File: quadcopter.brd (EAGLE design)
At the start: 130.1 x 130.1 mm, 75 parts, among them J1 AVR_SPI_PRG_6NS, J3 HEADER-0.1IN-2POS-FEMALE, J4 HEADER-0.1IN-2POS-FEMALE, J5 HEADER-0.1IN-2POS-FEMALE, J6 HEADER-0.1IN-2POS-FEMALE, SW1 PUSHBUTTON_SMD-VERTICAL, SW2 PUSHBUTTON_SMD-VERTICAL, U1 ATMEGA128RFA1

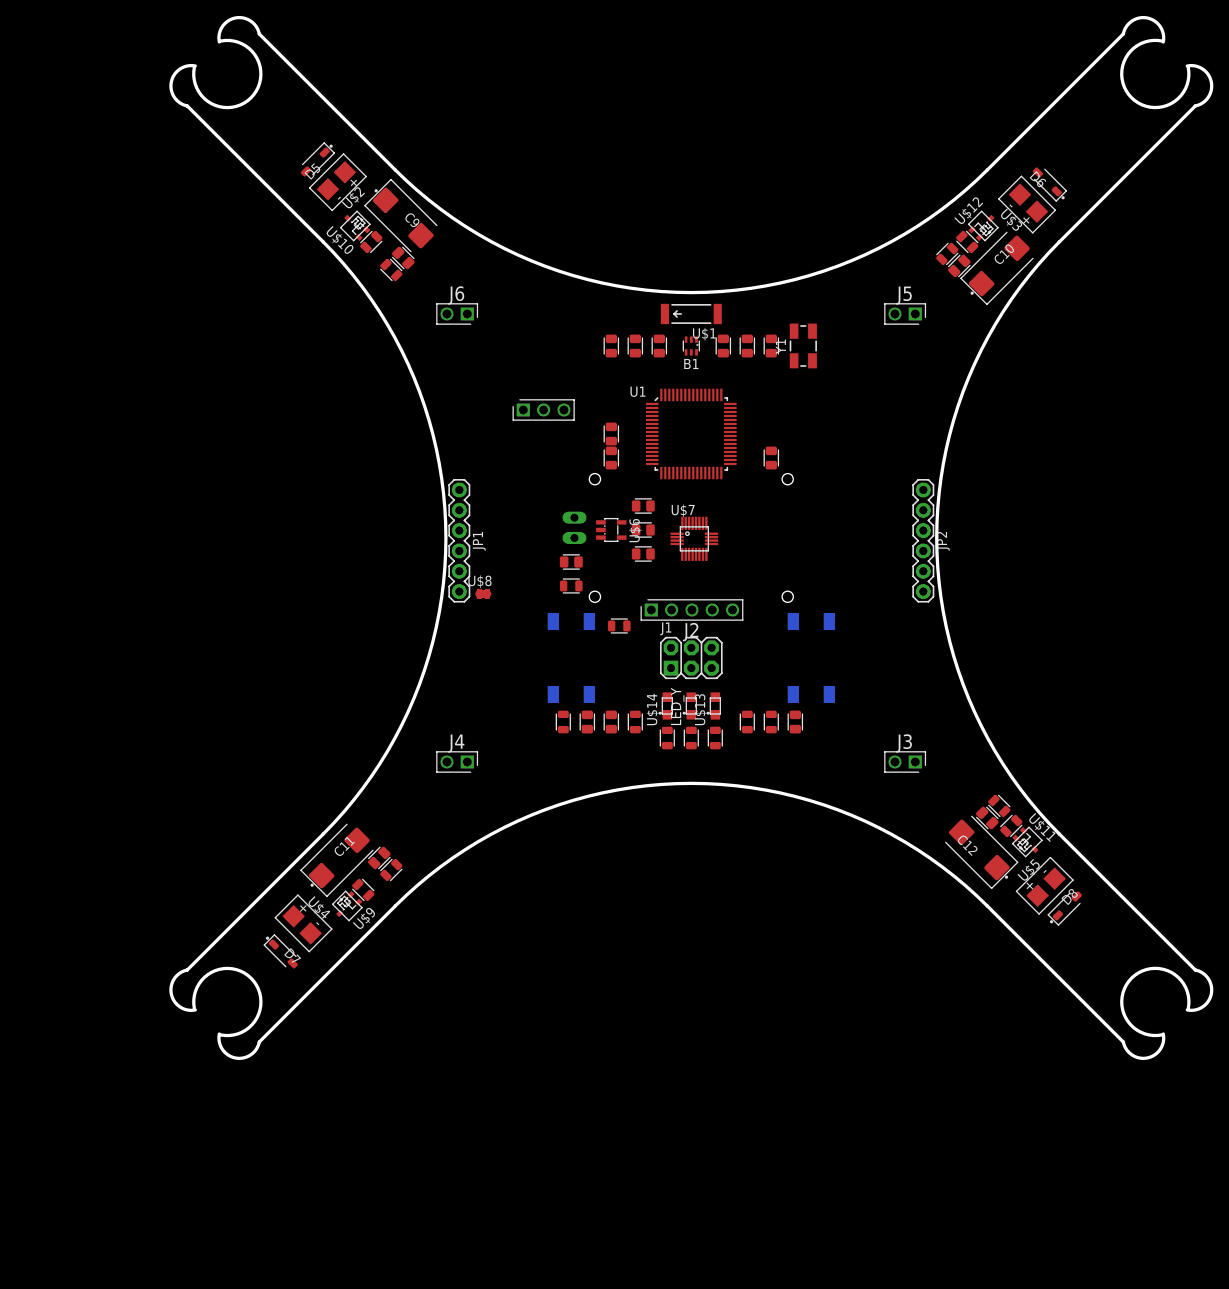
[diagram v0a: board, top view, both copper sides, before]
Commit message: Fixed n-fet and imu packages
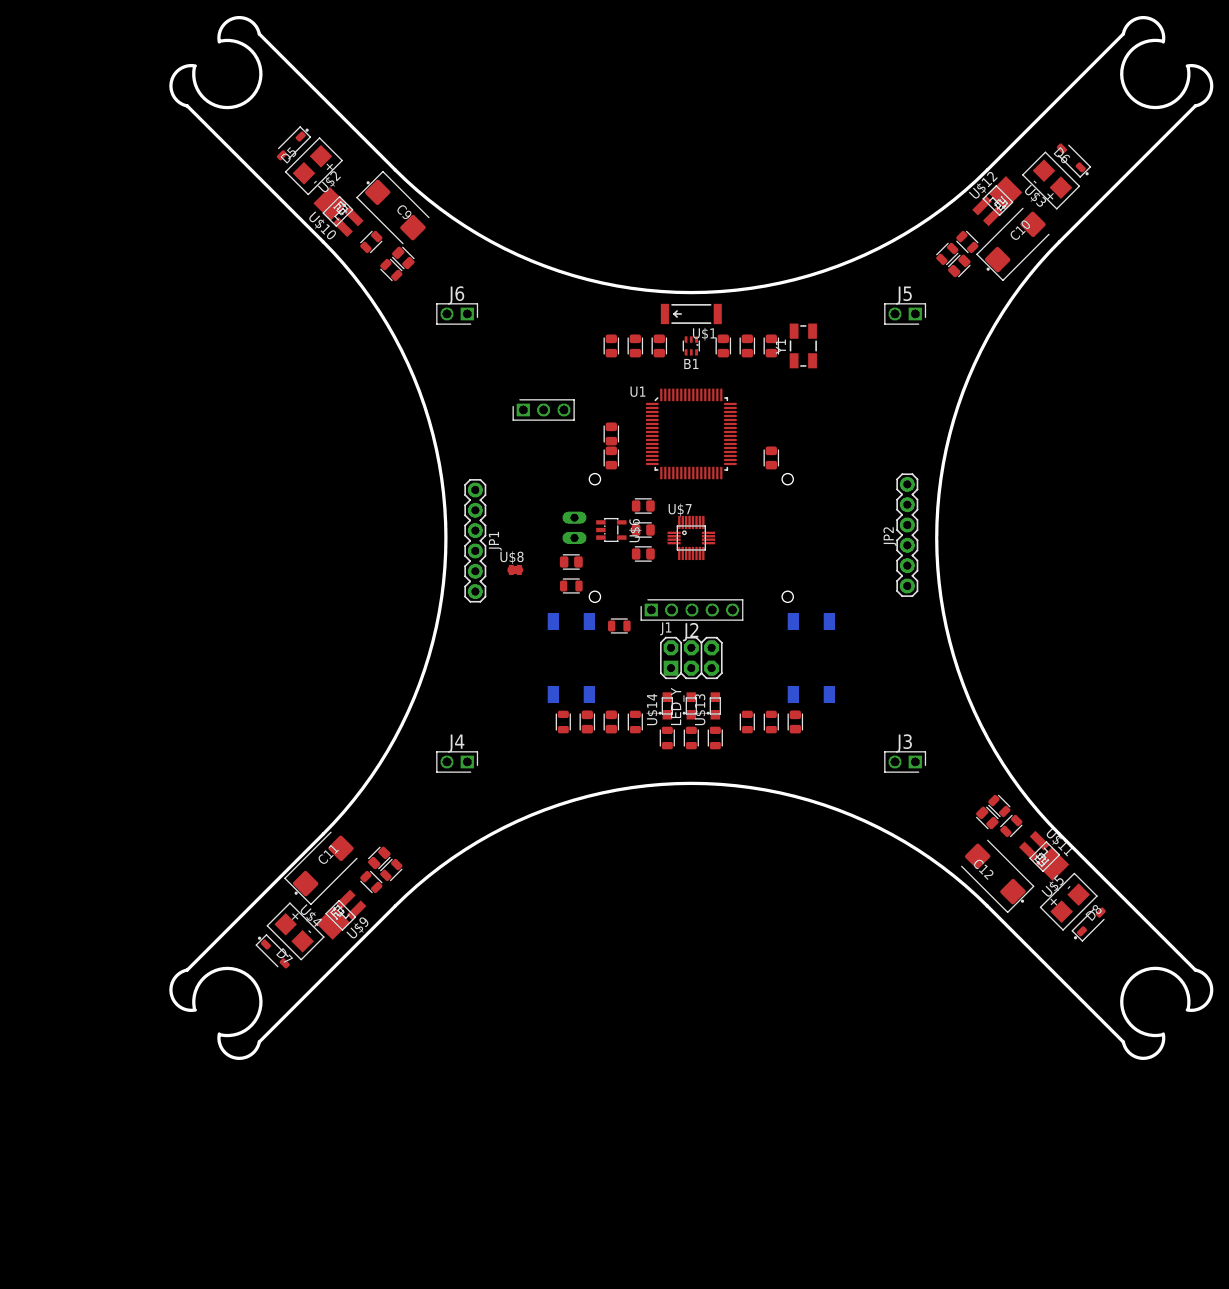
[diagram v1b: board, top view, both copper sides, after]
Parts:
- moved JP2 12.2 mm to (27.0, -6.00), turned to 90 degrees
- moved U$8 5.00 mm to (-22.0, -4.00)
- moved D6 4.24 mm to (47.5, 47.5)
- moved U$3 4.24 mm to (45.5, 44.5)
- moved C10 3.61 mm to (40.5, 37.0)
- moved C12 3.61 mm to (38.0, -42.0)
- moved D5 3.61 mm to (-50.0, 49.0)
- moved D8 3.61 mm to (50.0, -48.0)
- moved U$12 3.61 mm to (38.5, 42.0)
- moved U$2 3.61 mm to (-47.0, 47.0)
- moved U$5 3.61 mm to (47.0, -46.0)
- moved U$10 2.83 mm to (-44.0, 41.0)
- moved U$11 2.83 mm to (44.0, -40.0)
- moved C11 2.24 mm to (-46.0, -41.0)
- moved JP1 2.00 mm to (-27.0, 6.00)
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
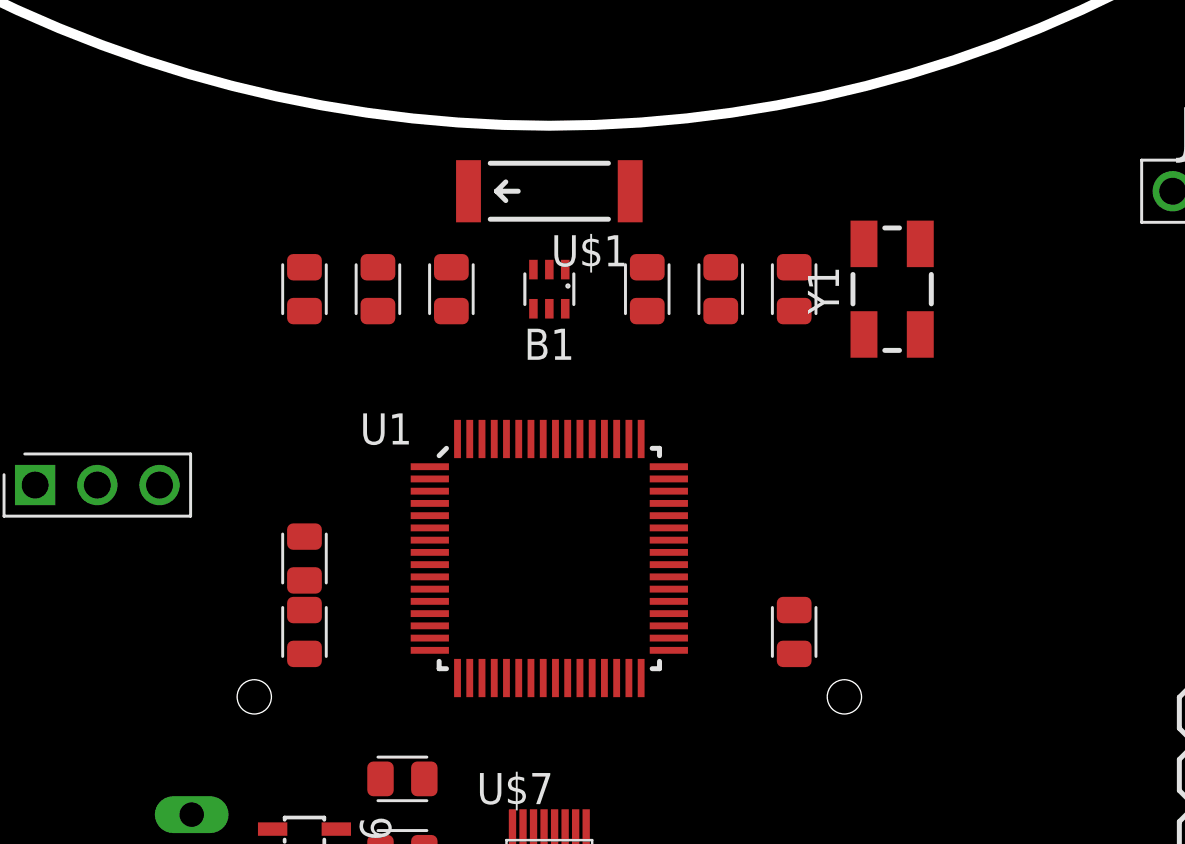
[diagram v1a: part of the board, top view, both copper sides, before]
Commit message: routed radio
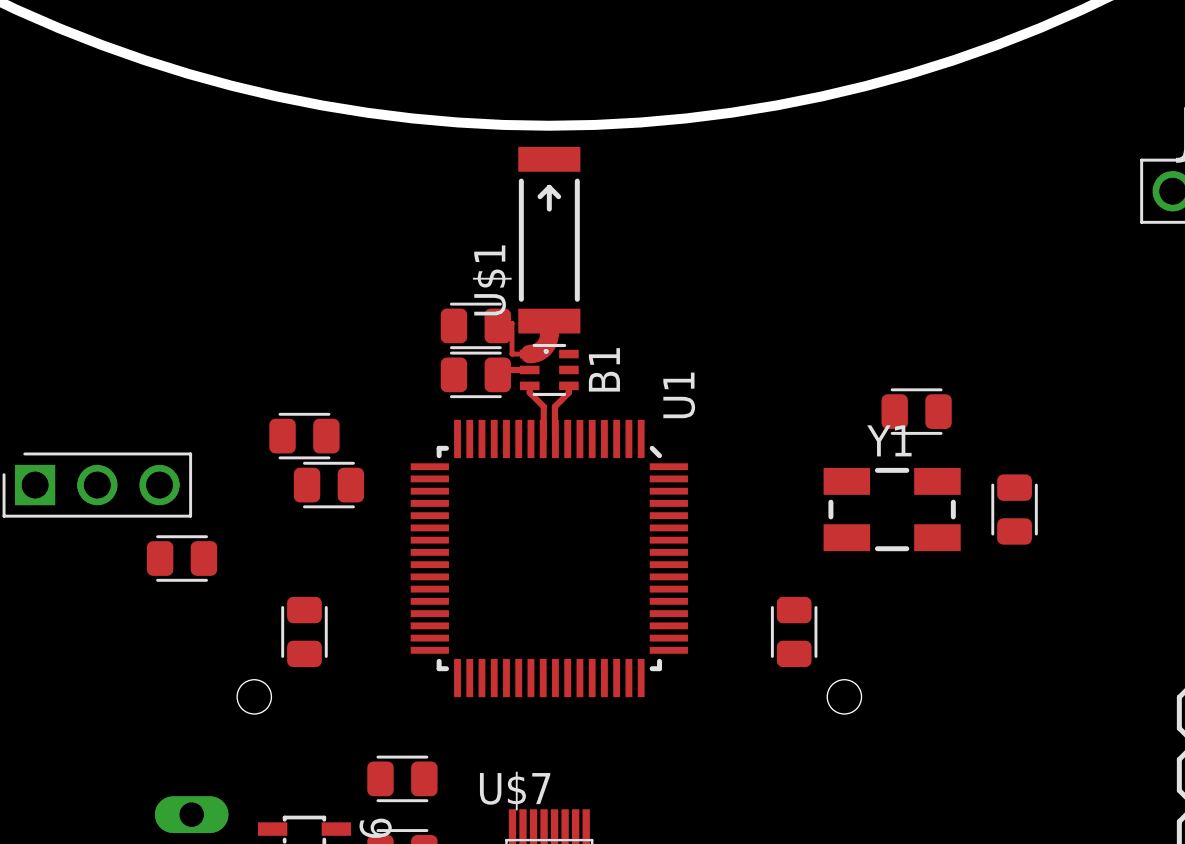
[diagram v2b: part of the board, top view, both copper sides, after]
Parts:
- moved C23 27.5 mm to (19.0, 15.0)
- moved C24 17.9 mm to (-9.00, 16.0), turned to 180 degrees
- moved Y1 9.00 mm to (14.0, 15.0), turned to 0 degrees
- moved C2 7.16 mm to (-3.00, 22.5), turned to 180 degrees
- moved C22 7.07 mm to (15.0, 19.0), turned to 180 degrees
- moved C25 6.00 mm to (-10.0, 18.0), turned to 0 degrees
- moved C4 5.00 mm to (-15.0, 13.0), turned to 0 degrees
- moved C1 3.64 mm to (-3.00, 20.5), turned to 0 degrees
- moved B1 3.30 mm to (0.00, 20.7), turned to 270 degrees
- moved U$1 2.00 mm to (0.00, 26.0), turned to 90 degrees
- turned U1 to 270 degrees
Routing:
- net ATTENNA: track 0.00 -> 4.35 mm
- net RFP: track 0.00 -> 2.41 mm
- net RFN: track 0.00 -> 2.41 mm
- net N$3: track 0.00 -> 1.50 mm

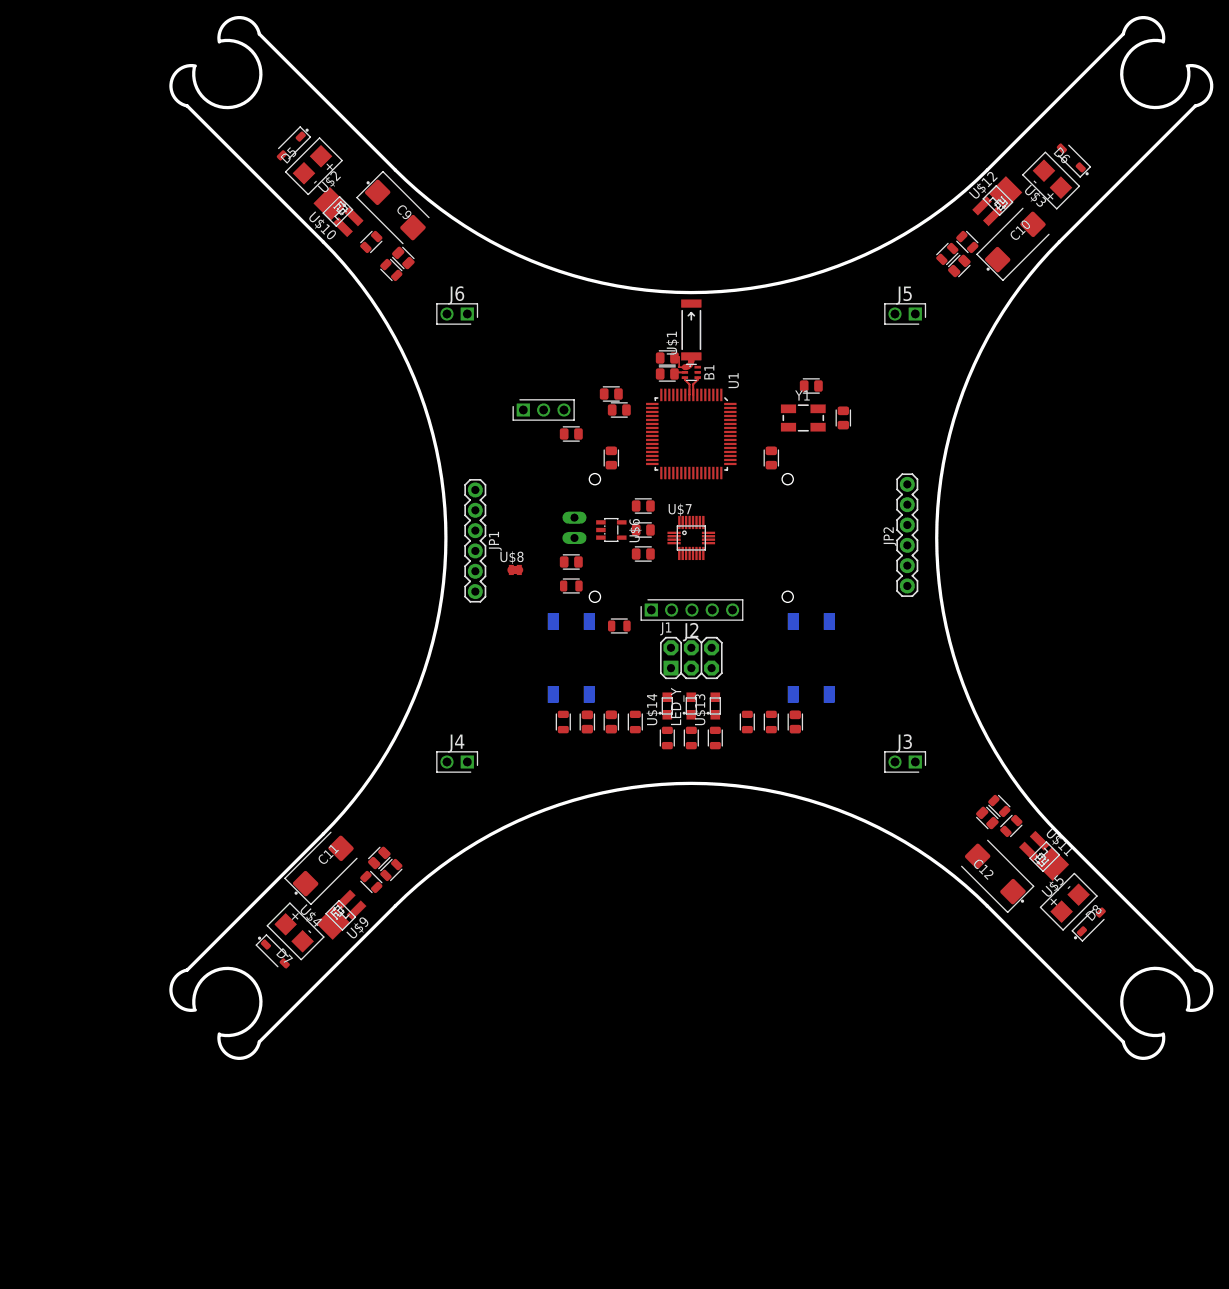
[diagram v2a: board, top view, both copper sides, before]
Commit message: added i2c pullups, placed oscillator components
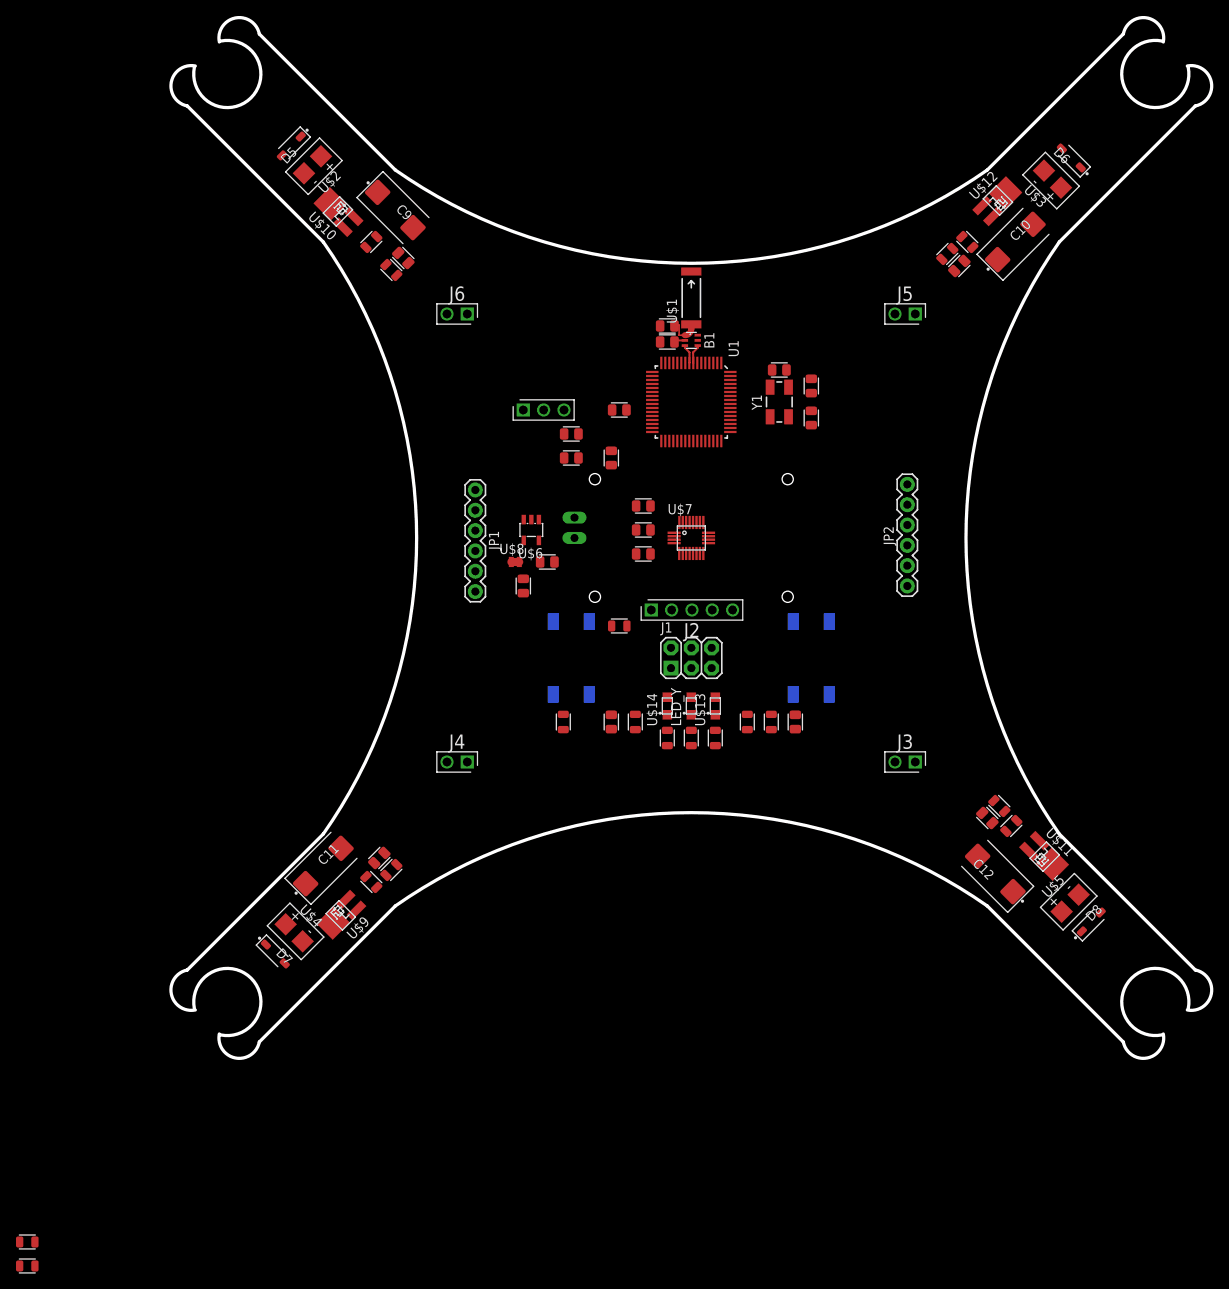
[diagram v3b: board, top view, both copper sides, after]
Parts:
- added R18: 10K, quadparts_prebuilt:RESC2012X60_HS
- moved R14 106.5 mm to (-83.0, -88.0), turned to 0 degrees
- moved C3 25.0 mm to (-15.0, 10.0), turned to 0 degrees
- moved C25 21.2 mm to (11.0, 21.0), turned to 180 degrees
- moved C16 18.8 mm to (-21.0, -6.00)
- moved U$6 10.0 mm to (-20.0, 1.00), turned to 180 degrees
- moved B1 4.00 mm to (0.00, 24.7)
- moved C1 4.00 mm to (-3.00, 24.5)
- moved C2 4.00 mm to (-3.00, 26.5)
- moved C23 4.00 mm to (15.0, 15.0)
- moved U$1 4.00 mm to (0.00, 30.0)
- moved U1 4.00 mm to (0.00, 17.0)
- moved Y1 3.61 mm to (11.0, 17.0), turned to 90 degrees
- moved C17 3.00 mm to (-18.0, -3.00), turned to 180 degrees
- moved U$8 1.00 mm to (-22.0, -3.00)
- turned C22 to 90 degrees
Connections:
- removed net N$10: R14.1, U$7.13, U$7.5, U$7.7, U$7.8
- net SCL: now also R14.2
- net SDA: now also R18.2
- net VCC: now also R14.1, R18.1, U$7.13, U$7.5, U$7.7, U$7.8; no longer R14.2
